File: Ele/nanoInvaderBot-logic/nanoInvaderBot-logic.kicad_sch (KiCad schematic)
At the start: 22 parts, among them J1 S6B-ZR-SM4A-TF(LF)(SN), J2 S6B-ZR-SM4A-TF(LF)(SN), J3 1746142-1, J4 Conn_01x20, P1 USB_C_Plug_USB2.0, U4 BQ25170DSGR, U5 TLV61048DBVT

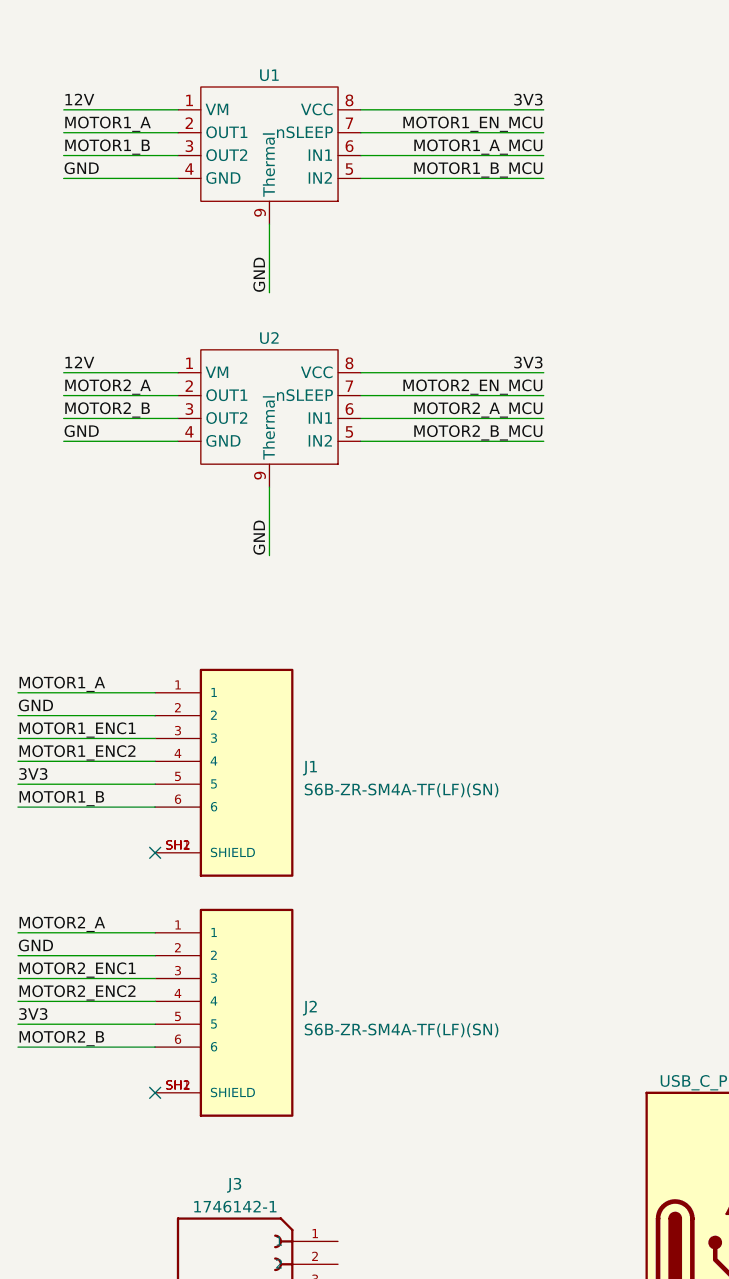
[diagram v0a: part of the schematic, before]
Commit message: Power side done, logic side cleanup
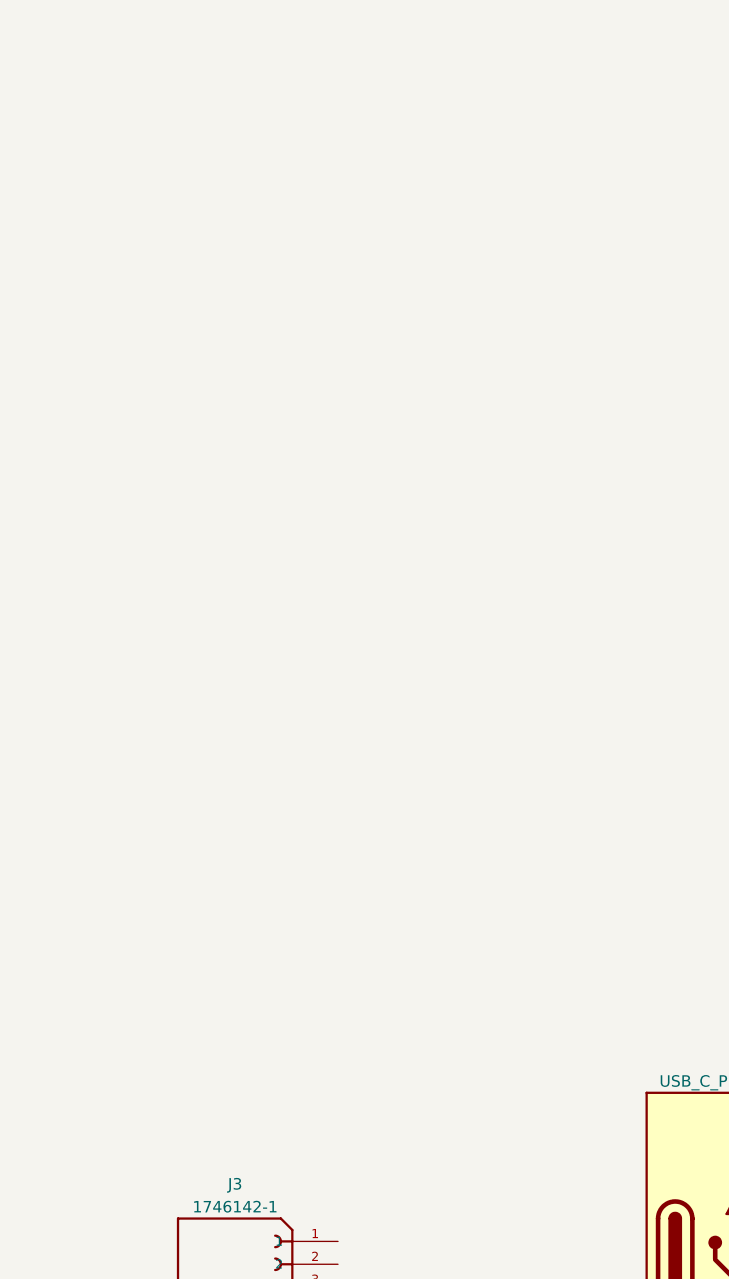
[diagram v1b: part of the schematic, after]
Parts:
- removed J1, J2: S6B-ZR-SM4A-TF(LF)(SN), footprints:JST_S6B-ZR-SM4A-TF(LF)(SN), symbol S6B-ZR-SM4A-TF_LF__SN_:S6B-ZR-SM4A-TF(LF)(SN)
- removed U1, U2: ~, Package_SON:WSON-8-1EP_2x2mm_P0.5mm_EP0.9x1.6mm, symbol DRV8212:DRV8212
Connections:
- no-connect marks 6 -> 4

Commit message: Intermediate state after v23.10
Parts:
- removed D1, D2: LED, LED_SMD:LED_0603_1608Metric, symbol Device:LED
- removed D3: D, symbol Device:D
- removed J3: 1746142-1, footprints:TE_1746142-1, symbol 1746142-1:1746142-1
- removed P1: USB_C_Plug_USB2.0, Connector_USB:USB_C_Receptacle_GCT_USB4135-GF-A_6P_TopMnt_Horizontal, symbol Connector:USB_C_Plug_USB2.0
- removed U3: ~, Package_TO_SOT_SMD:SOT-23-5, symbol XC8111:XC8111-MR-G
- removed U4: BQ25170DSGR, footprints:BQ25170DSGR_NV, symbol BQ25170DSGR:BQ25170DSGR
- removed U5: TLV61048DBVT, SOT23-6_DBV_TEX, symbol TLV61048DBVT:TLV61048DBVT
- added C3: C, Capacitor_SMD:C_0603_1608Metric, symbol Device:C
- added C4, C5: 100n, Capacitor_SMD:C_0603_1608Metric, symbol Device:C
- added C6, C7, C8: C, Capacitor_SMD:C_0805_2012Metric, symbol Device:C
- added J1: USB4110-GF-A, footprints:USB4110-GF-A_GCT, symbol USB4110-GF-A:USB4110-GF-A
- added Q1, Q2: BC817W, Package_TO_SOT_SMD:SOT-323_SC-70, symbol Transistor_BJT:BC817W
- added R1, R11, R12, R13, R4: R, Resistor_SMD:R_0402_1005Metric, symbol Device:R
- added R2: 24k, Resistor_SMD:R_0402_1005Metric, symbol Device:R
- added R3: 47k, Resistor_SMD:R_0402_1005Metric, symbol Device:R
- added U1: CP2102N-Axx-xQFN28, Package_DFN_QFN:QFN-28-1EP_5x5mm_P0.5mm_EP3.35x3.35mm, symbol Interface_USB:CP2102N-Axx-xQFN28
- added U2: ESP32-C3-MINI-1-N4, footprints:XCVR_ESP32-C3-MINI-1-N4, symbol ESP32-C3-MINI-1-N4:ESP32-C3-MINI-1-N4
- added U3: LSM6DS3, Package_LGA:LGA-14_3x2.5mm_P0.5mm_LayoutBorder3x4y, symbol Sensor_Motion:LSM6DS3
- added U5: TPS631000DRLR, footprints:SOTFL50P160X60-8N, symbol TPS631000DRLR:TPS631000DRLR
- C1, C2: footprint (none) -> Capacitor_SMD:C_0805_2012Metric
- L1: value L -> DFE252012P-1R0M=P2; footprint (none) -> Inductor_SMD:L_2512_6332Metric
- R10: value R -> 91k; footprint (none) -> Resistor_SMD:R_0402_1005Metric
- R5, R6, R7, R8: footprint Resistor_SMD:R_0603_1608Metric -> Resistor_SMD:R_0402_1005Metric
- R9: value R -> 510k; footprint (none) -> Resistor_SMD:R_0402_1005Metric
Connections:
- net 3V3: now also C2.1, J4.10 (Pin_10), R5.1, R9.1, C4.1, C5.1, C6.2, C7.2, C8.2, R1.1, R12.1, R13.1, U1.6 (VDD), U1.7 (VREGIN), U2.3 (3V3), U3.12 (CS), U3.5 (VDDIO), U3.8 (VDD), U5.1 (VOUT)
- net GND: now also R10.2, R7.2, C3.2, C4.2, C5.2, C6.1, C7.1, C8.1, J1.A1-B12 (GND), J1.A12-B1 (GND), R11.2, R3.2, U1.29 (GND), U1.3 (GND), U2.1 (GND), U2.11 (GND), U2.14 (GND), U2.2 (GND), U2.36 (GND), U2.37 (GND), U2.38 (GND), U2.39 (GND), U2.40 (GND), U2.41 (GND), U2.42 (GND), U2.43 (GND), U2.44 (GND), U2.45 (GND), U2.46 (GND), U2.47 (GND), U2.48 (GND), U2.49_1 (GND), U2.49_2 (GND), U2.49_3 (GND), U2.49_4 (GND), U2.49_5 (GND), U2.49_6 (GND), U2.49_7 (GND), U2.49_8 (GND), U2.49_9 (GND), U2.50 (GND), U2.51 (GND), U2.52 (GND), U2.53 (GND), U3.1 (SDO/SA0), U3.2 (SDX), U3.3 (SCX), U3.6 (GND), U3.7 (GND), U5.7 (GND); no longer J4.10 (Pin_10), R5.2, R9.2
- net MOTOR1_A_MCU: now also J4.6 (Pin_6), U2.13 (IO1); no longer J4.7 (Pin_7)
- net MOTOR1_B_MCU: now also J4.5 (Pin_5), U2.12 (IO0); no longer J4.8 (Pin_8)
- net MOTOR1_ENC1: now also J4.8 (Pin_8), U2.6 (IO3); no longer J4.5 (Pin_5)
- net MOTOR1_ENC2: now also J4.9 (Pin_9), U2.18 (IO4); no longer J4.6 (Pin_6)
- net MOTOR1_EN_MCU: now also J4.7 (Pin_7), U2.16 (IO10); no longer J4.9 (Pin_9)
- net MOTOR2_A_MCU: now also J4.15 (Pin_15), U2.21 (IO7); no longer J4.14 (Pin_14)
- net MOTOR2_B_MCU: now also J4.14 (Pin_14), U2.20 (IO6); no longer J4.13 (Pin_13)
- net MOTOR2_ENC1: now also J4.12 (Pin_12), U2.27 (IO19); no longer J4.15 (Pin_15)
- net MOTOR2_ENC2: now also J4.13 (Pin_13), U2.26 (IO18); no longer J4.16 (Pin_16)
- net MOTOR2_EN_MCU: now also J4.16 (Pin_16), U2.19 (IO5); no longer J4.12 (Pin_12)
- net VSYS: now also U5.4 (VIN), U5.5 (EN), U5.6 (MODE); no longer L1.2
- net VUSB: now also J1.A4-B9 (VBUS), J1.A9-B4 (VBUS), R2.1
- net at R6.1: now also J1.B5 (CC2)
- net at R8.2: now also Q2.1 (B)
- net at L1.1: now also U5.2 (LX2)
- net 12V: no longer names the net of R10.1
- net 12V: now also R9.2, U5.8 (FB); no longer C2.1
- net VBATT: no longer names the net of R7.1
- net VBATT: now also J1.A5 (CC1); no longer R8.1
- new net: R11.1, U1.11 (~{SUSPEND})
- new net: R2.2, R3.1, U1.8 (VBUS)
- new net: L1.2, U5.3 (LX1)
- new net: R1.2, U1.9 (~{RST})
- new net: U2.10 (NC), U2.15 (NC), U2.17 (NC), U2.24 (NC), U2.25 (NC), U2.28 (NC), U2.29 (NC), U2.32 (NC), U2.33 (NC), U2.34 (NC), U2.35 (NC), U2.4 (NC), U2.7 (NC), U2.9 (NC)
- new net: Q1.1 (B), R4.2
- new net CHIP_PU: C3.1, Q1.3 (C), R5.2, U2.8 (EN)
- new net DTR: Q2.3 (C), R4.1, U1.28 (~{DTR})
- new net GPIO9: Q2.2 (E), U2.23 (IO9)
- new net IMU_SCL: R12.2, U2.22 (IO8), U3.13 (SCL)
- new net IMU_SDA: R13.2, U2.5 (IO2), U3.14 (SDA)
- new net RTS: Q1.2 (E), R8.1, U1.24 (~{RTS})
- new net USB_DN: J1.A7 (DN1), J1.B7 (DN2), U1.5 (D-)
- new net USB_DP: J1.A6 (DP1), J1.B6 (DP2), U1.4 (D+)
- new net USB_RX: U1.25 (RXD), U2.31 (TXD0)
- new net USB_TX: U1.26 (TXD), U2.30 (RXD0)
- no-connect marks 4 -> 19
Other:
- moved on the sheet: J4

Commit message: Modifications for first running proto
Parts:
- R1, R11: value R -> 10k
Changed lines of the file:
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@@
       (effects (font (size 1.27 1.27)) (justify left))
     )
-    (property "Value" "R" (at 87.63 118.745 0)
+    (property "Value" "10k" (at 87.63 118.745 0)
       (effects (font (size 1.27 1.27)) (justify left))
     )
@@
       (effects (font (size 1.27 1.27)) (justify left))
     )
-    (property "Value" "R" (at 45.72 80.645 0)
-      (effects (font (size 1.27 1.27)) (justify left))
-    )
+    (property "Value" "10k" (at 45.72 80.645 0)
+      (effects (font (size 1.27 1.27)) (justify left))
+    )
